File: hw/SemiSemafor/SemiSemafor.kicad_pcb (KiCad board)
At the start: 2 copper layers, 15.8 x 30 mm, 24 parts, among them J1 USB_PCB, SW1 SW_DIP_x01, U1 LD39200, U2 ESP32-C3-MINI-1

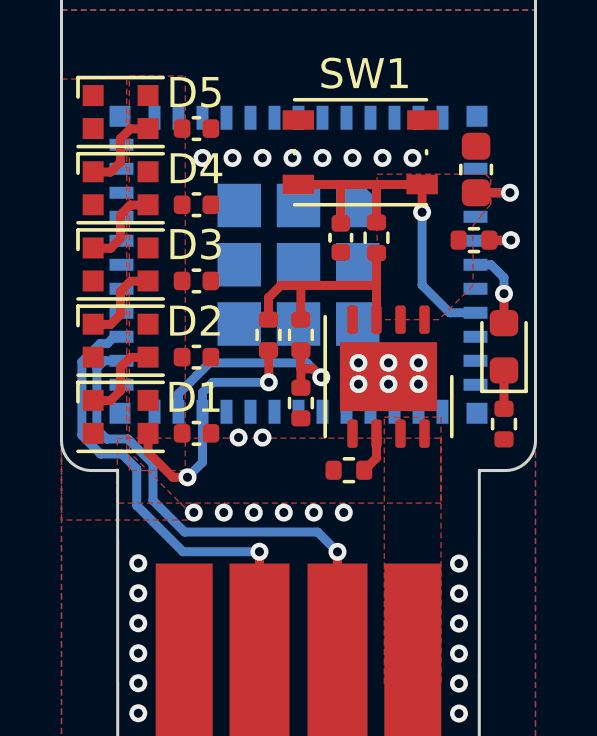
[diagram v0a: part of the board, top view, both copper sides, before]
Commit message: Change button connection
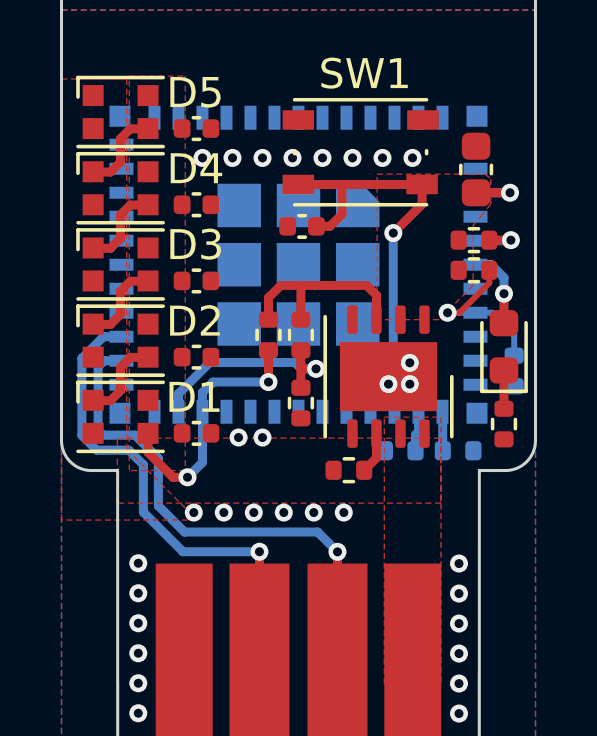
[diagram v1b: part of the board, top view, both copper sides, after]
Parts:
- added R14: nc, Resistor_SMD:R_0402_1005Metric, B.Cu at (157.2, 107.7)
- added R8: nc, Resistor_SMD:R_0402_1005Metric, B.Cu at (155.3, 110.3)
- added R9: nc, Resistor_SMD:R_0402_1005Metric, B.Cu at (153.4, 110.3)
- moved R5 3.43 mm to (155.8, 104.3), turned to 180 degrees
- moved C8 1.34 mm to (150.1, 102.9), turned to 180 degrees
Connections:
- C8 pad 1: /EN -> /GPIO10
- SW1 pad 2: /EN -> /GPIO10
- U2 pad 12: unconnected-(U2-Pad12) -> Net-(R8-Pad2)
- U2 pad 13: unconnected-(U2-Pad13) -> Net-(R9-Pad2)
- U2 pad 16: unconnected-(U2-Pad16) -> /GPIO10
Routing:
- net /GPIO10: track 0.00 -> 14.8 mm, vias 0 -> 1
- net /EN: track 12.2 -> 5.45 mm
- net Net-(R9-Pad2): track 0.00 -> 1.34 mm
- net Net-(R8-Pad2): track 0.00 -> 1.30 mm
- net +3.3V: track 10.1 -> 8.87 mm
- net /GPIO9: track 8.03 -> 7.46 mm
- net GND: vias 34 -> 31
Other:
- board text added: "EN"

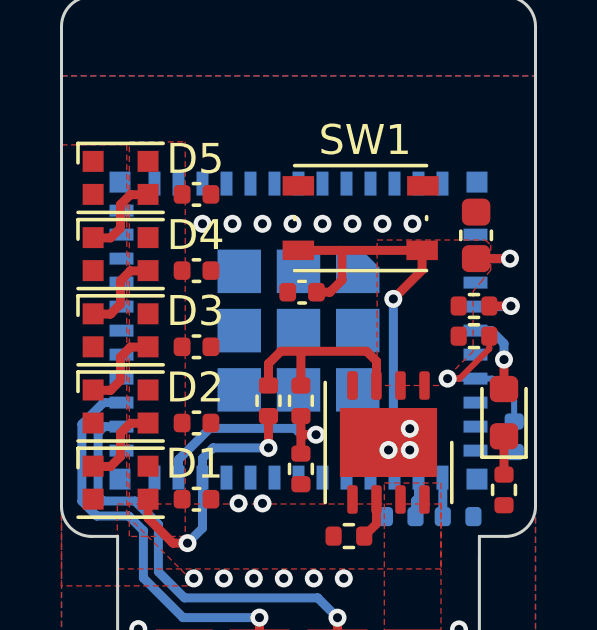
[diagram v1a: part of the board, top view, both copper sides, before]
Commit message: fix LDO
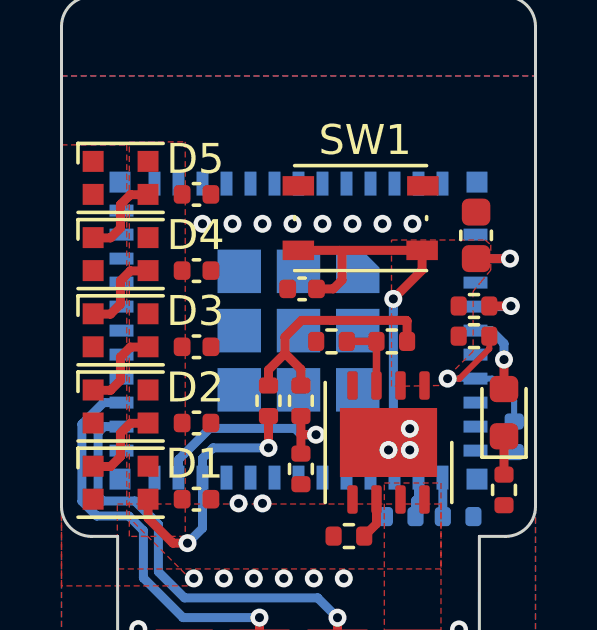
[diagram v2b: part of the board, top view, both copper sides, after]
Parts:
- added R10: 10k, Resistor_SMD:R_0402_1005Metric, F.Cu at (151.1, 104.5)
- added R11: 62k, Resistor_SMD:R_0402_1005Metric, F.Cu at (153.1, 104.5)
- moved C8 0.11 mm to (150.1, 102.8)
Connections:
- U1 pad 3: +3.3V -> Net-(U1-Pad3)
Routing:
- net Net-(U1-Pad3): track 0.00 -> 2.46 mm
- net +3.3V: track 8.87 -> 10.3 mm

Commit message: PCB
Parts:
- removed D6: IR-LED, LED_SMD:LED_0603_1608Metric
- removed R1: 10k, Resistor_SMD:R_0402_1005Metric
- removed R14, R7, R8, R9: nc, Resistor_SMD:R_0402_1005Metric
- removed R6: 100, Resistor_SMD:R_0402_1005Metric
- added C7: 1u, Capacitor_SMD:C_0402_1005Metric, B.Cu at (154.0, 105.7)
- added FB1: FerriteBead, Inductor_SMD:L_0201_0603Metric, F.Cu at (143.1, 97.5)
- added J2: ESP-Programing_conector, Robotarna_KiCad_Library:ESP-Programing_conector, F.Cu at (156.2, 109.4)
- added SW2: SW_DIP_x01, Button_Switch_SMD:SW_Push_1P1T_NO_Vertical_Wuerth_434133025816, F.Cu at (145.0, 102.0)
- C6, C8, R10, R2, R3, R4, R5, U1: moved to B.Cu
- R11: value 62k -> 56k; moved to B.Cu
- moved D1 14.0 mm to (144.8, 95.3), turned to -90 degrees
- moved C1 12.2 mm to (144.3, 97.8), turned to -90 degrees
- moved C6 12.1 mm to (145.2, 106.6), turned to 180 degrees
- moved D2 11.9 mm to (147.4, 95.3), turned to -90 degrees
- moved D5 11.6 mm to (155.0, 95.3), turned to -90 degrees
- moved D3 10.6 mm to (149.9, 95.3), turned to -90 degrees
- moved D4 10.5 mm to (152.5, 95.3), turned to -90 degrees
- moved C2 9.42 mm to (146.8, 97.8), turned to -90 degrees
- moved C5 8.05 mm to (154.4, 97.8), turned to -90 degrees
- moved C3 7.42 mm to (149.4, 97.8), turned to -90 degrees
- moved C4 6.86 mm to (151.9, 97.8), turned to -90 degrees
- moved R4 6.38 mm to (157.3, 97.1), turned to 90 degrees
- moved C8 5.96 mm to (155.3, 105.7), turned to -90 degrees
- moved U2 5.14 mm to (150.0, 99.0)
- moved R2 4.80 mm to (145.4, 105.2), turned to 180 degrees
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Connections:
- net /GPIO9 renamed /BOOT
- C8 pad 1: /GPIO10 -> /SW0
- D1 pad 3: /GPIO8 -> Net-(D1-Pad3)
- R3 pad 1: /GPIO8 -> /I-LED
- SW1 pad 2: /GPIO10 -> /SW0
- U1 pad 6: Net-(R1-Pad2) -> +5V
- U2 pad 11: (no net) -> GND
- U2 pad 12: Net-(R8-Pad2) -> /SW0
- U2 pad 13: Net-(R9-Pad2) -> /SW1
- U2 pad 14: (no net) -> GND
- U2 pad 16: /GPIO10 -> unconnected-(U2-Pad16)
- U2 pad 2: (no net) -> GND
- U2 pad 22: /GPIO8 -> /I-LED
- U2 pad 30: unconnected-(U2-Pad30) -> /RX0
- U2 pad 31: unconnected-(U2-Pad31) -> /TX0
- U2 pad 36: (no net) -> GND
- U2 pad 37: (no net) -> GND
- U2 pad 38: (no net) -> GND
- U2 pad 39: (no net) -> GND
- U2 pad 40: (no net) -> GND
- U2 pad 41: (no net) -> GND
- U2 pad 42: (no net) -> GND
- U2 pad 43: (no net) -> GND
- U2 pad 44: (no net) -> GND
- U2 pad 45: (no net) -> GND
- U2 pad 46: (no net) -> GND
- U2 pad 47: (no net) -> GND
- U2 pad 48: (no net) -> GND
- U2 pad 49: (no net) -> GND
- U2 pad 6: /GPIO3 -> unconnected-(U2-Pad6)
- U2 pad 7: (no net) -> +3.3V
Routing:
- net /SW1: track 0.00 -> 16.5 mm, vias 0 -> 1
- net +3.3V: track 10.3 -> 25.3 mm, vias 1 -> 4
- net /GPIO10: track 14.7 -> 0.00 mm, vias 1 -> 0
- net /TX0: track 0.00 -> 12.9 mm, vias 0 -> 1
- net /RX0: track 0.00 -> 12.6 mm, vias 0 -> 1
- net /I-LED: track 0.00 -> 9.46 mm, vias 0 -> 1
- net /GPIO8: track 8.73 -> 0.00 mm, vias 2 -> 0
- net +5V: track 0.00 -> 8.49 mm, vias 0 -> 7
- net /SW0: track 0.00 -> 8.29 mm, vias 0 -> 1
- net /EN: track 5.45 -> 12.8 mm
- net /USB-D+: track 16.8 -> 19.6 mm, vias 1 -> 3
- net /GPIO3: track 2.65 -> 0.00 mm, vias 1 -> 0
- net /USB-D-: track 17.7 -> 20.0 mm, vias 1 -> 3
- net Net-(D1-Pad3): track 0.00 -> 1.94 mm
- net Net-(R1-Pad2): track 1.39 -> 0.00 mm
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- added copper zone on B.Cu, net +3.3V
- added copper zone on B.Cu, net +5V
- removed copper zone on F.Cu, net +3.3V
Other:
- board size 15.8 x 30 mm -> 15.8 x 35.1 mm

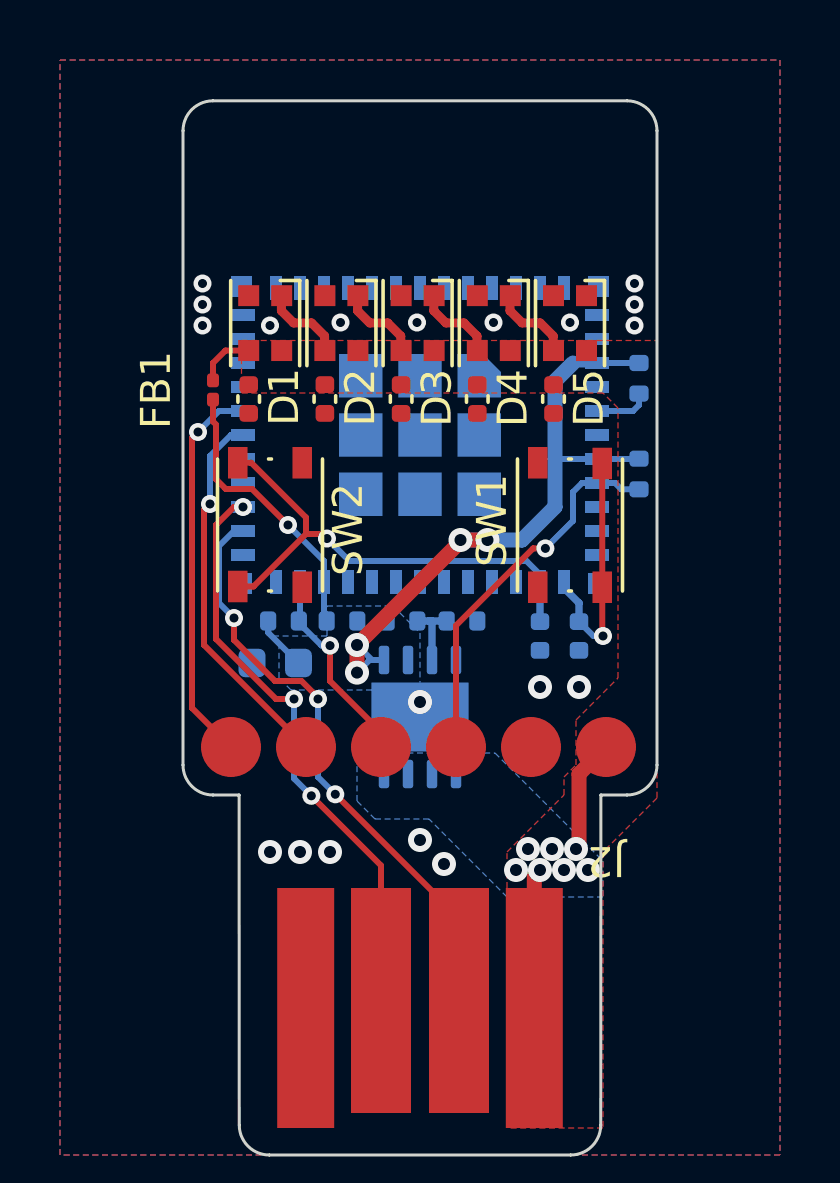
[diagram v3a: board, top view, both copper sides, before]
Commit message: Polygon and rout tracks correction
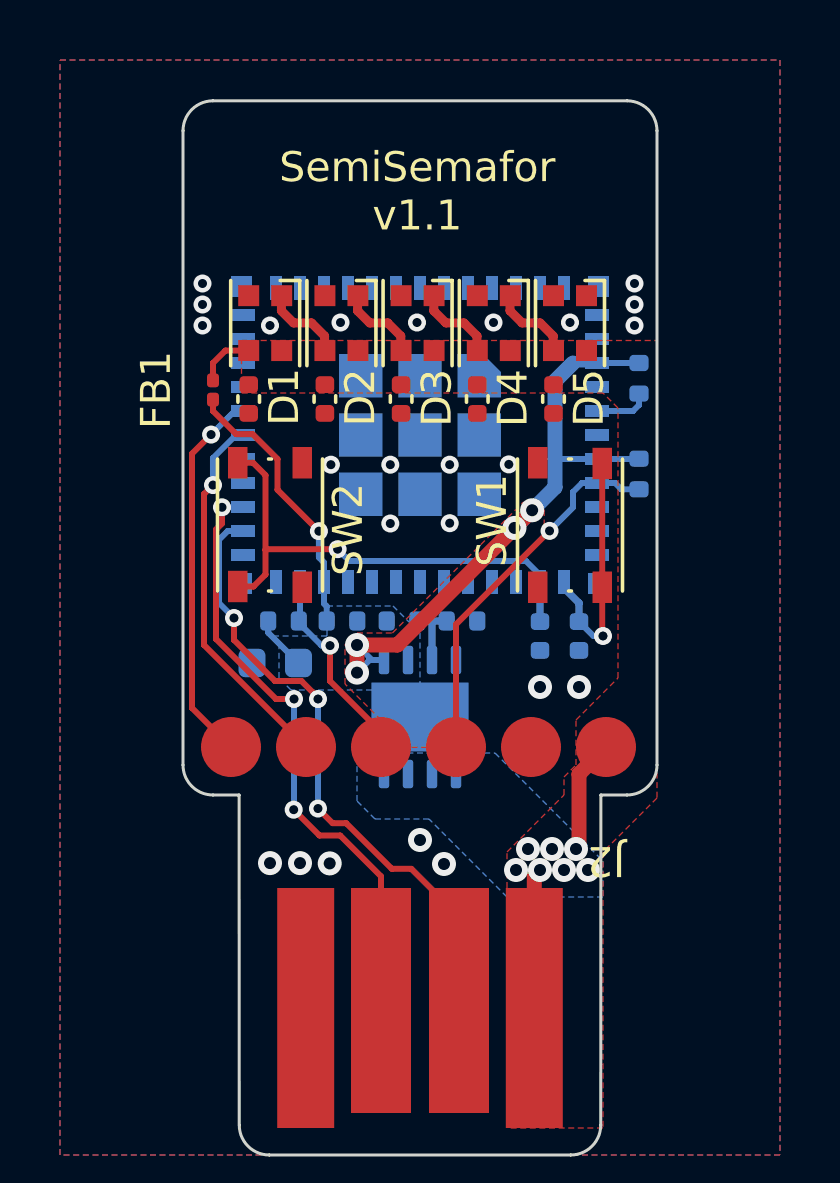
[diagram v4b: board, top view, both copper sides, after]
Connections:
- U2 pad 50: (no net) -> GND
- U2 pad 51: (no net) -> GND
- U2 pad 52: (no net) -> GND
- U2 pad 53: (no net) -> GND
- U2 pad 7: +3.3V -> (no net)
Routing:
- net /USB-D-: track 20.0 -> 20.8 mm
- net /USB-D+: track 19.6 -> 20.3 mm
- net GND: vias 19 -> 24
- added copper zone on F.Cu, net +3.3V
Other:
- board text added: "SemiSemafor v1.1"

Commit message: V2.0 (Circuit)
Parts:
- added C10: 1u, Capacitor_SMD:C_0402_1005Metric, F.Cu at (149.4, 61.9)
- added C11: 1u, Capacitor_SMD:C_0402_1005Metric, F.Cu at (158.6, 64.0)
- added C12: 1u, Capacitor_SMD:C_0402_1005Metric, F.Cu at (165.4, 70.4)
- added C13: 1u, Capacitor_SMD:C_0402_1005Metric, F.Cu at (168.2, 79.5)
- added C14: 1u, Capacitor_SMD:C_0402_1005Metric, F.Cu at (166.0, 88.6)
- added C15: 1u, Capacitor_SMD:C_0402_1005Metric, F.Cu at (159.6, 95.4)
- added C9: 1u, Capacitor_SMD:C_0402_1005Metric, F.Cu at (140.4, 64.6)
- added D10: WS2812B, LED_SMD:LED_WS2812B-2020_PLCC4_2.0x2.0mm, F.Cu at (165.6, 80.0)
- added D11: WS2812B, LED_SMD:LED_WS2812B-2020_PLCC4_2.0x2.0mm, F.Cu at (163.5, 87.8)
- added D12: WS2812B, LED_SMD:LED_WS2812B-2020_PLCC4_2.0x2.0mm, F.Cu at (157.8, 93.5)
- added D6: WS2812B, LED_SMD:LED_WS2812B-2020_PLCC4_2.0x2.0mm, F.Cu at (142.2, 66.5)
- added D7: WS2812B, LED_SMD:LED_WS2812B-2020_PLCC4_2.0x2.0mm, F.Cu at (150.0, 64.4)
- added D8: WS2812B, LED_SMD:LED_WS2812B-2020_PLCC4_2.0x2.0mm, F.Cu at (157.8, 66.5)
- added D9: WS2812B, LED_SMD:LED_WS2812B-2020_PLCC4_2.0x2.0mm, F.Cu at (163.5, 72.2)
- added svg2mod: G***, RKL-Graphic:RobotarnaLogo-6mm, F.Cu at (150.0, 80.0)
- moved C5 33.4 mm to (134.0, 71.4), turned to 150 degrees
- moved D5 29.6 mm to (136.5, 72.2), turned to 150 degrees
- moved C4 26.5 mm to (131.8, 80.5), turned to 180 degrees
- moved D4 23.7 mm to (134.4, 80.0), turned to 180 degrees
- moved C3 17.0 mm to (134.6, 89.6), turned to -150 degrees
- moved D3 15.4 mm to (136.5, 87.8), turned to -150 degrees
- moved FB1 6.38 mm to (149.4, 98.2)
- moved C1 6.27 mm to (150.6, 98.2)
- moved C2 5.72 mm to (141.4, 96.0), turned to -120 degrees
- moved D2 5.47 mm to (142.2, 93.5), turned to -120 degrees
- moved D1 5.17 mm to (150.0, 95.6)
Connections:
- net /SW0 renamed /SW2
- D5 pad 1: unconnected-(D5-Pad1) -> Net-(D5-DOUT)
- U2 pad 7: (no net) -> +3.3V
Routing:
- net Net-(D6-DOUT): track 0.00 -> 10.3 mm
- net Net-(D10-DIN): track 0.00 -> 10.3 mm
- net Net-(D11-DOUT): track 0.00 -> 10.3 mm
- net Net-(D5-DOUT): track 0.00 -> 10.3 mm
- net Net-(D8-DOUT): track 0.00 -> 10.3 mm
- net Net-(D7-DOUT): track 0.00 -> 10.3 mm
- net Net-(D10-DOUT): track 0.00 -> 10.3 mm
- net Net-(D3-DOUT): track 2.78 -> 10.3 mm
- net Net-(D4-DOUT): track 2.78 -> 10.3 mm
- net Net-(D2-DOUT): track 2.78 -> 10.2 mm
- net Net-(D1-DOUT): track 2.78 -> 9.96 mm
- net /I-LED: track 9.27 -> 8.01 mm
- net +5V: track 8.49 -> 9.65 mm
- net Net-(D1-DIN): track 1.94 -> 1.31 mm
- net GND: vias 24 -> 25
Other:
- board size 15.8 x 35.1 mm -> 40.2 x 63.1 mm
- board text added: "SW1"
- board text added: "SW2"
- board text added: "SemiSemafor v2.0"
- board text removed: "SemiSemafor v1.1"

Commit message: Logo
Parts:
- moved svg2mod 8.00 mm to (150.0, 72.0)
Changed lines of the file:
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@@
   )
   (footprint "RKL-Graphic:RobotarnaLogo-6mm" (layer "F.Cu")
-    (at 150 80)
+    (at 150 72)
     (descr "Imported from /home/xmrazek7/Stažené/robotarna_logo_pcb.svg")
     (tags "svg2mod")
@@
     )
     (stroke (width 0.2) (type default)) (fill none) (layer "F.SilkS"))
-  (gr_circle (center 150 80) (end 153.5 80)
-    (stroke (width 0.15) (type default)) (fill none) (layer "F.SilkS"))
   (gr_poly
     (pts
@@
   (gr_line (start 157.9 88.86) (end 157.9 99.9)
     (stroke (width 0.1) (type default)) (layer "F.SilkS"))
-  (gr_rect (start 136.9 77.5) (end 131.9 82.5)
+  (gr_rect (start 131.9 77.5) (end 136.9 82.5)
     (stroke (width 0.2) (type default)) (fill none) (layer "F.SilkS"))
-  (gr_rect (start 152.5 66.9) (end 147.5 61.9)
+  (gr_rect (start 147.5 61.9) (end 152.5 66.9)
     (stroke (width 0.2) (type default)) (fill none) (layer "F.SilkS"))
-  (gr_rect (start 163.1 82.5) (end 168.1 77.5)
+  (gr_rect (start 163.1 77.5) (end 168.1 82.5)
     (stroke (width 0.2) (type default)) (fill none) (layer "F.SilkS"))
   (gr_arc (start 156.9 87.86) (mid 157.607106 88.152893) (end 157.9 88.86)

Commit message: Logo
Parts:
- removed svg2mod: G***, RKL-Graphic:RobotarnaLogo-6mm
